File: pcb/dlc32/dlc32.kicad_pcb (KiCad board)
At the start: 2 copper layers, 99.8 x 43.9 mm, 62 parts, among them IC1 74HCT08, IC2 74HCT14, J1 DOOR1, J10 CHILLER SSR PWR, J11 EXHAUST, J12 EXT1, J13 COM2, J14 DLC32:J18, J15 INT PWR, J16 TP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

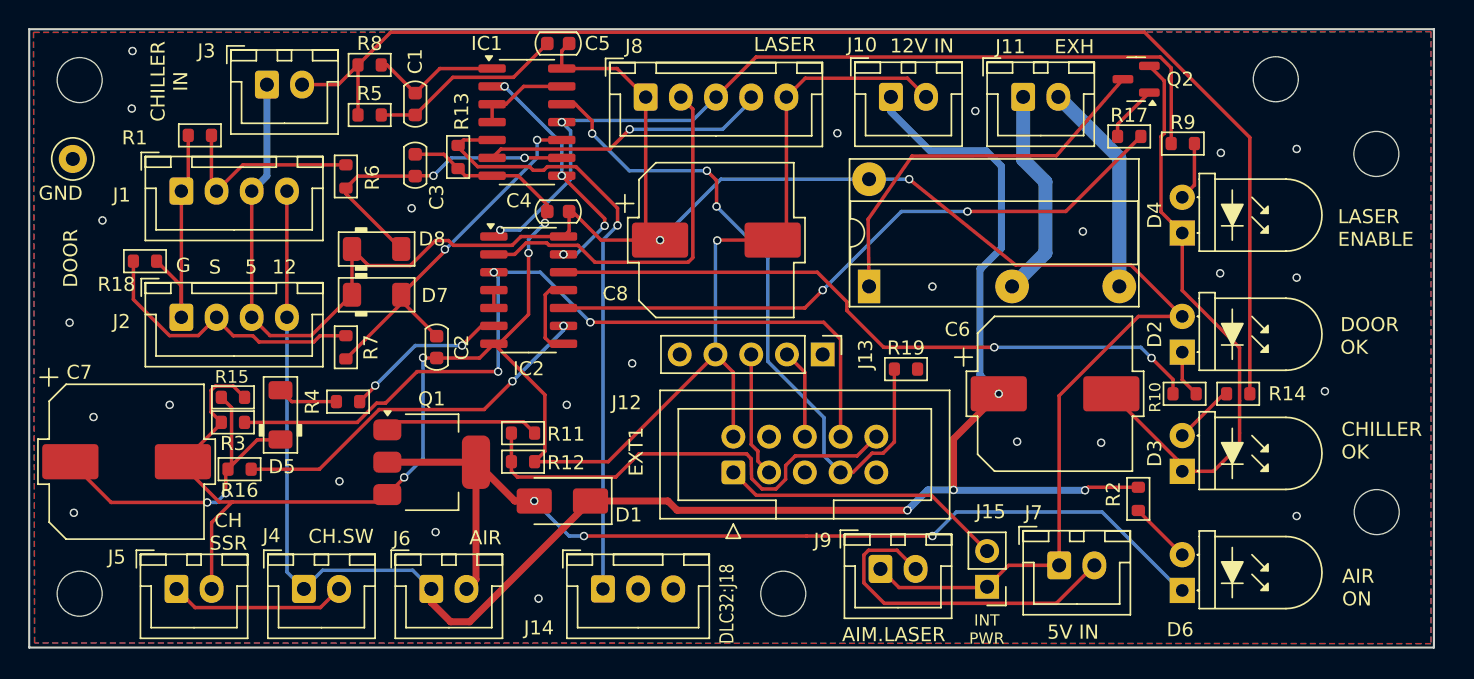
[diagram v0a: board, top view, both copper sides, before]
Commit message: Change to tantalum cap. Optimize connector placement.
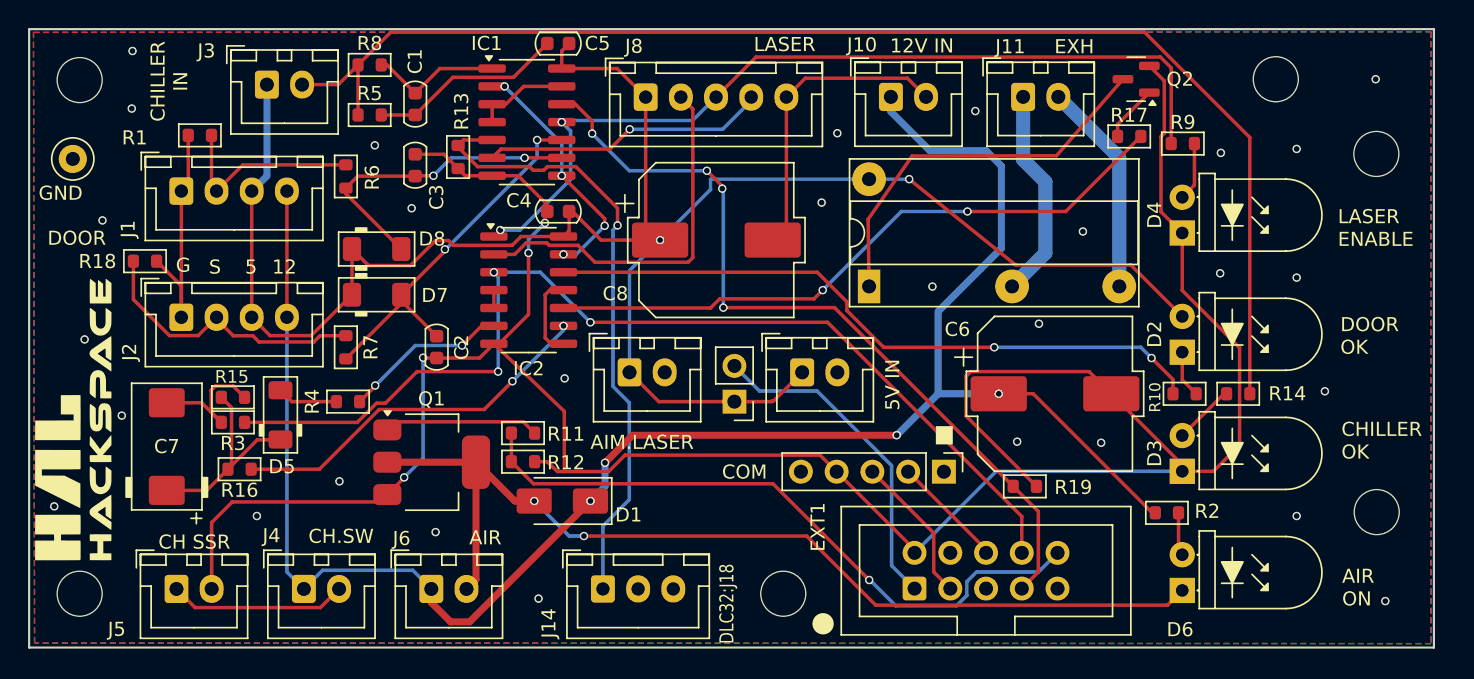
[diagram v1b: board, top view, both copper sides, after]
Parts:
- added G***: LOGO, hal9k:hal9k-logo_20mm, F.Cu at (77.0, 52.1)
- C7: footprint PCM_Capacitor_SMD_AKL:CP_Elec_10x10 -> PCM_Capacitor_Tantalum_SMD_AKL:CP_EIA-7343-15_Kemet-W
- moved J7 22.8 mm to (128.8, 48.8)
- moved J9 22.7 mm to (116.6, 48.8)
- moved J15 22.3 mm to (124.0, 50.9)
- moved J12 15.3 mm to (136.8, 64.1)
- moved J13 12.0 mm to (138.9, 55.8)
- moved R19 11.9 mm to (144.7, 56.9)
- moved C7 3.05 mm to (83.7, 54.0), turned to 90 degrees
- moved R2 2.26 mm to (154.8, 58.8), turned to 0 degrees
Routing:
- net VALVE_CTRL: track 33.4 -> 47.2 mm, vias 0 -> 1
- net FAN: track 60.2 -> 74.0 mm
- net +5V: track 154.3 -> 141.9 mm
- net GND: track 236.6 -> 247.4 mm, vias 30 -> 33
- net Net-(D5-K): track 24.3 -> 15.0 mm, vias 2 -> 0
- net LASER_EN: track 48.1 -> 57.4 mm, vias 3 -> 4
- net Net-(J12-Pin_1): track 20.3 -> 23.5 mm
- net RX: track 8.91 -> 10.6 mm
- net TX: track 6.37 -> 8.06 mm
- net Net-(D6-A): track 4.44 -> 3.09 mm
- net +V_VALVE: track 132.7 -> 131.7 mm
- net LASER_PWM: track 43.5 -> 44.5 mm
- net Net-(D1-A): track 71.0 -> 70.5 mm, vias 3 -> 2
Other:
- board text added: "."
- board text added: "COM"
- board text removed: "INT PWR"

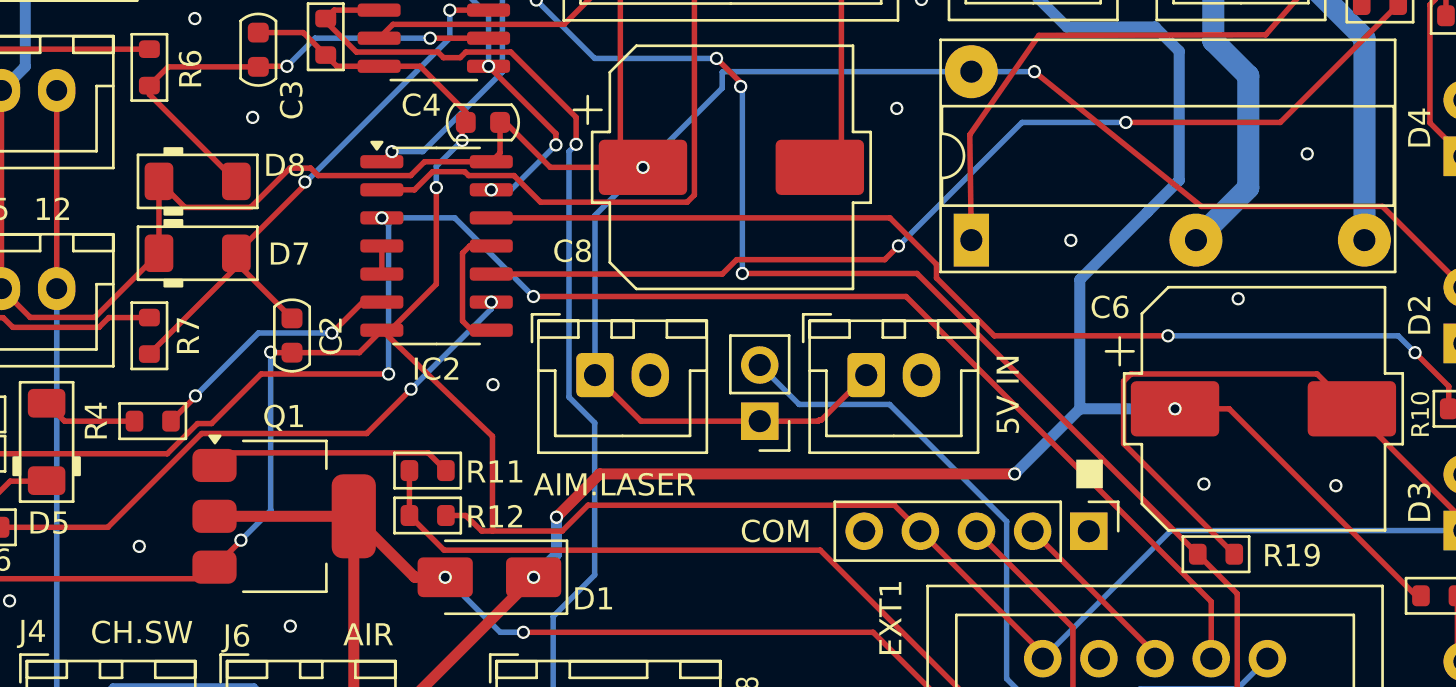
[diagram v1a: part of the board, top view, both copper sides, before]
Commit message: Save grblHAL settings, reorganize datasheets.
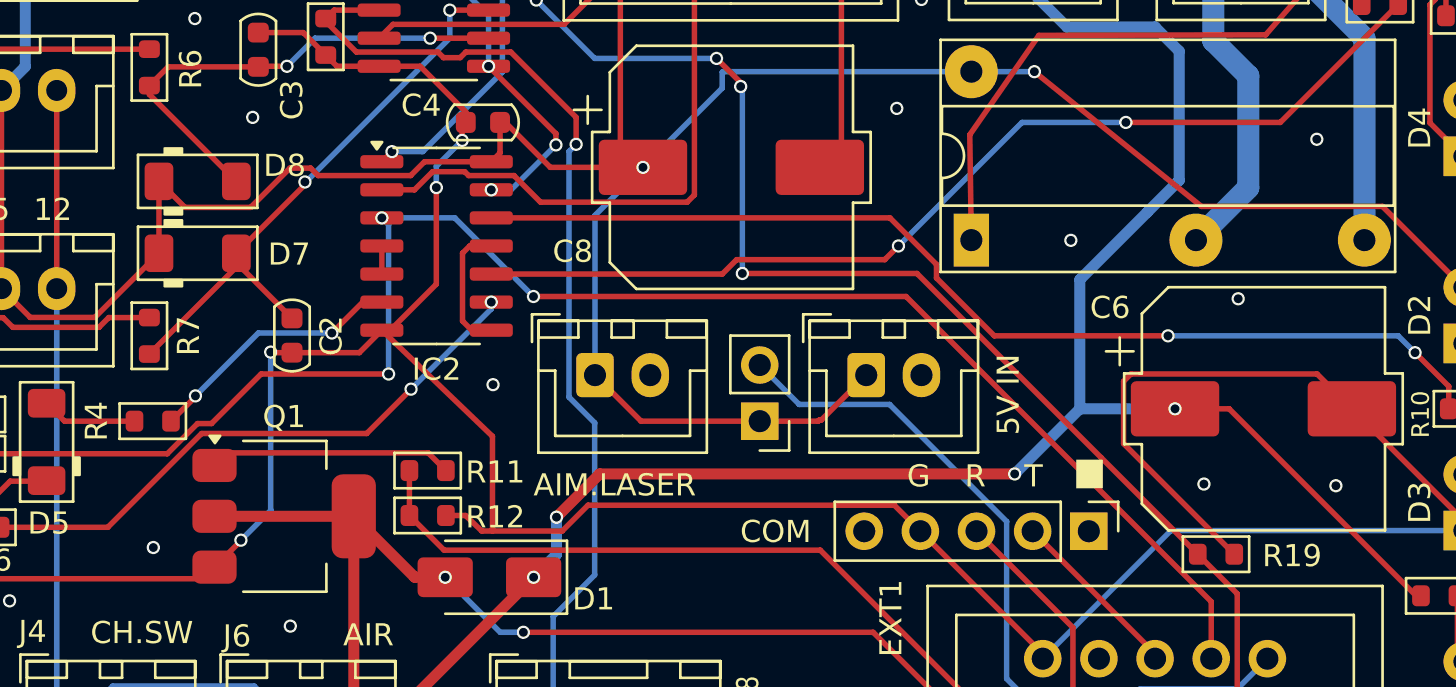
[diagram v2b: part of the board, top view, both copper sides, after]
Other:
- board text added: "R"
- board text added: "T"

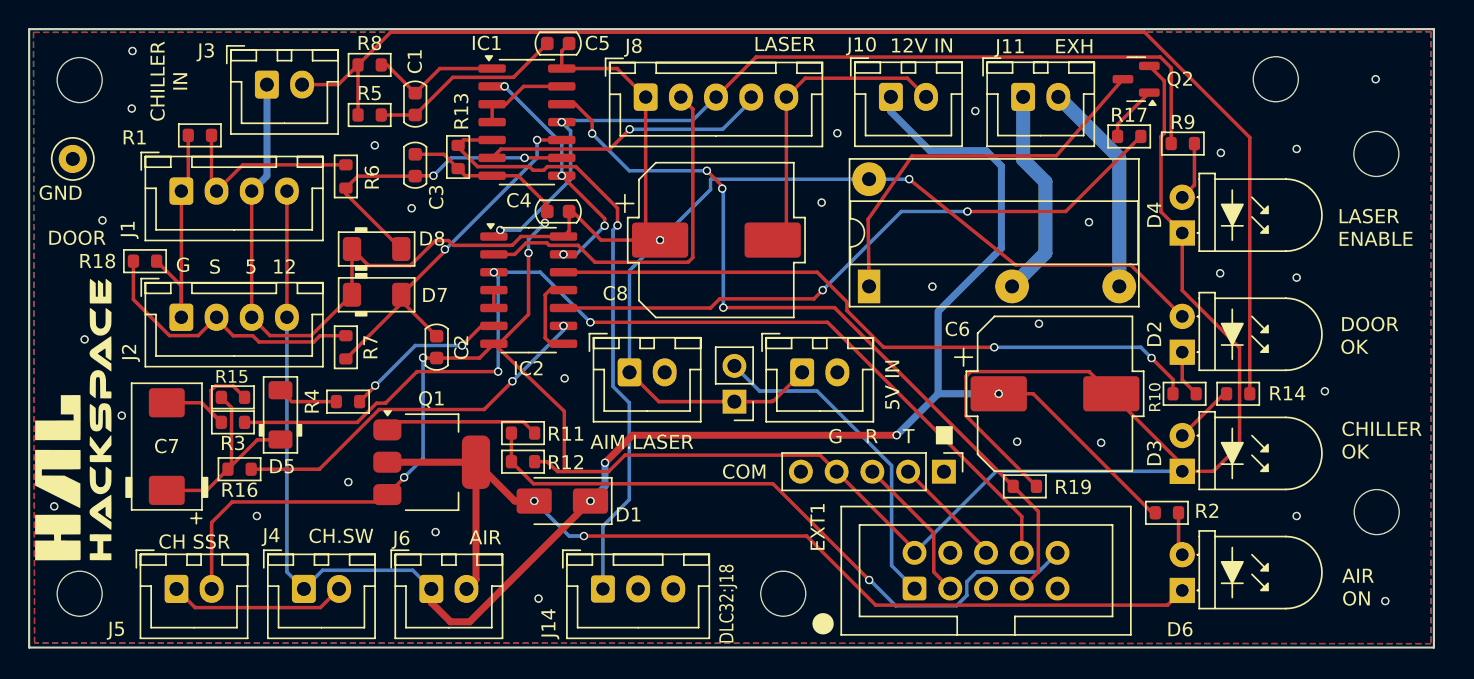
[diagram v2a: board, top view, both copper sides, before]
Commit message: Eliminate LASER_EN.
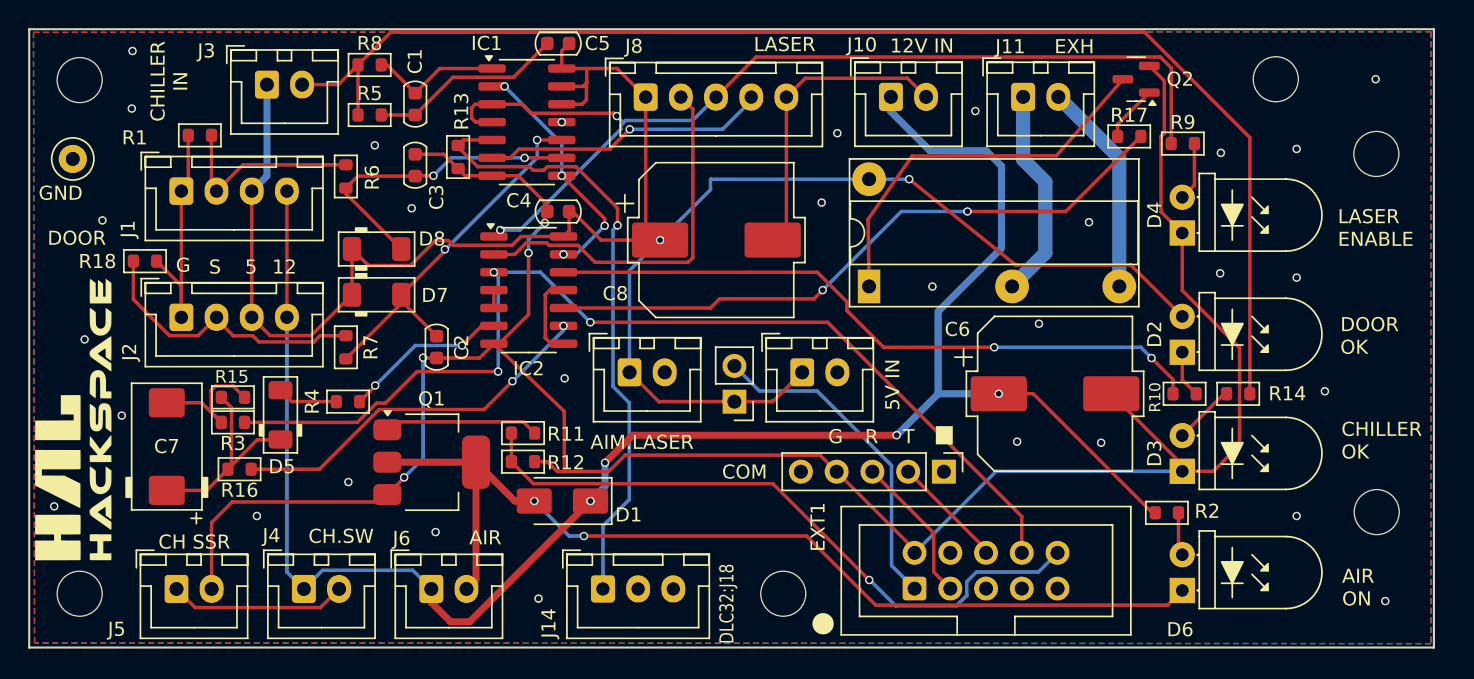
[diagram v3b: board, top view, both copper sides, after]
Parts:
- removed R19: 10k, PCM_Resistor_SMD_AKL:R_0603_1608Metric
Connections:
- IC1 pad 11: Net-(J8-Pin_3) -> unconnected-(IC1-Pad11)
- IC1 pad 12: LASER_EN -> +5V
- IC1 pad 13: Net-(IC1-Pad13) -> +5V
- IC1 pad 3: Net-(IC1-Pad13) -> Net-(J8-Pin_3)
- IC1 pad 4: Net-(IC1-Pad13) -> Net-(J8-Pin_3)
- J12 pad 7: LASER_EN -> unconnected-(J12-Pin_7-Pad7)
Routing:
- net LASER_EN: track 57.4 -> 0.00 mm, vias 4 -> 0
- net GND: track 247.4 -> 226.4 mm
- net Net-(J8-Pin_3): track 62.4 -> 73.4 mm
- net Net-(IC1-Pad13): track 6.75 -> 0.00 mm
- net +5V: track 141.9 -> 147.9 mm
- net unconnected-(IC1-Pad11): track 0.00 -> 0.17 mm, vias 0 -> 1

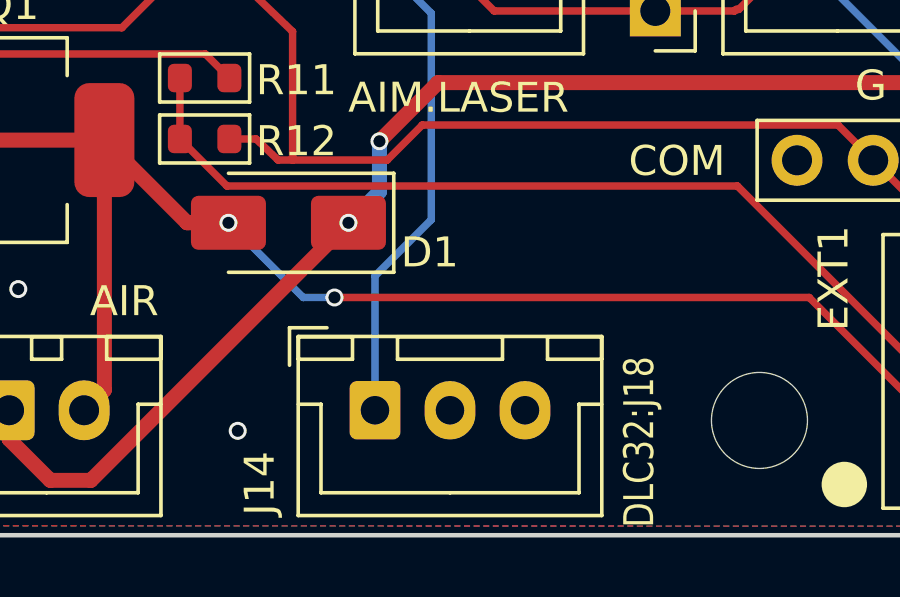
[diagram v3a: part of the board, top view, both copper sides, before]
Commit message: Use correct pin on DLC32:J18.
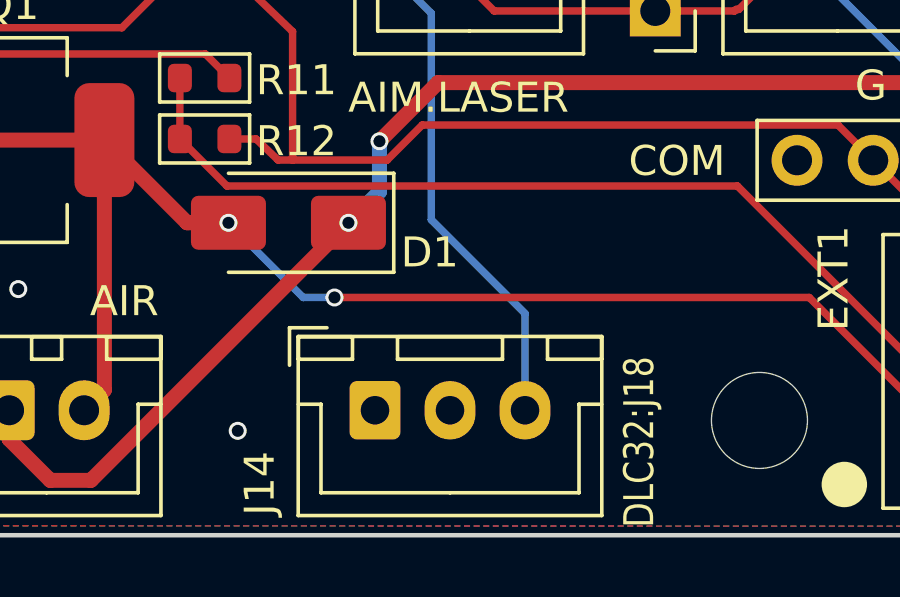
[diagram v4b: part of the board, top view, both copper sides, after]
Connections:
- J14 pad 1: LASER_PWM -> unconnected-(J14-Pin_1-Pad1)
- J14 pad 3: unconnected-(J14-Pin_3-Pad3) -> LASER_PWM
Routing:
- net LASER_PWM: track 44.5 -> 45.0 mm
